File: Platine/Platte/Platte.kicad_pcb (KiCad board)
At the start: 2 copper layers, 32.6 x 32.6 mm, 21 parts, among them J1 Conn_01x07_MountingPin, J3 Conn_01x04_Socket

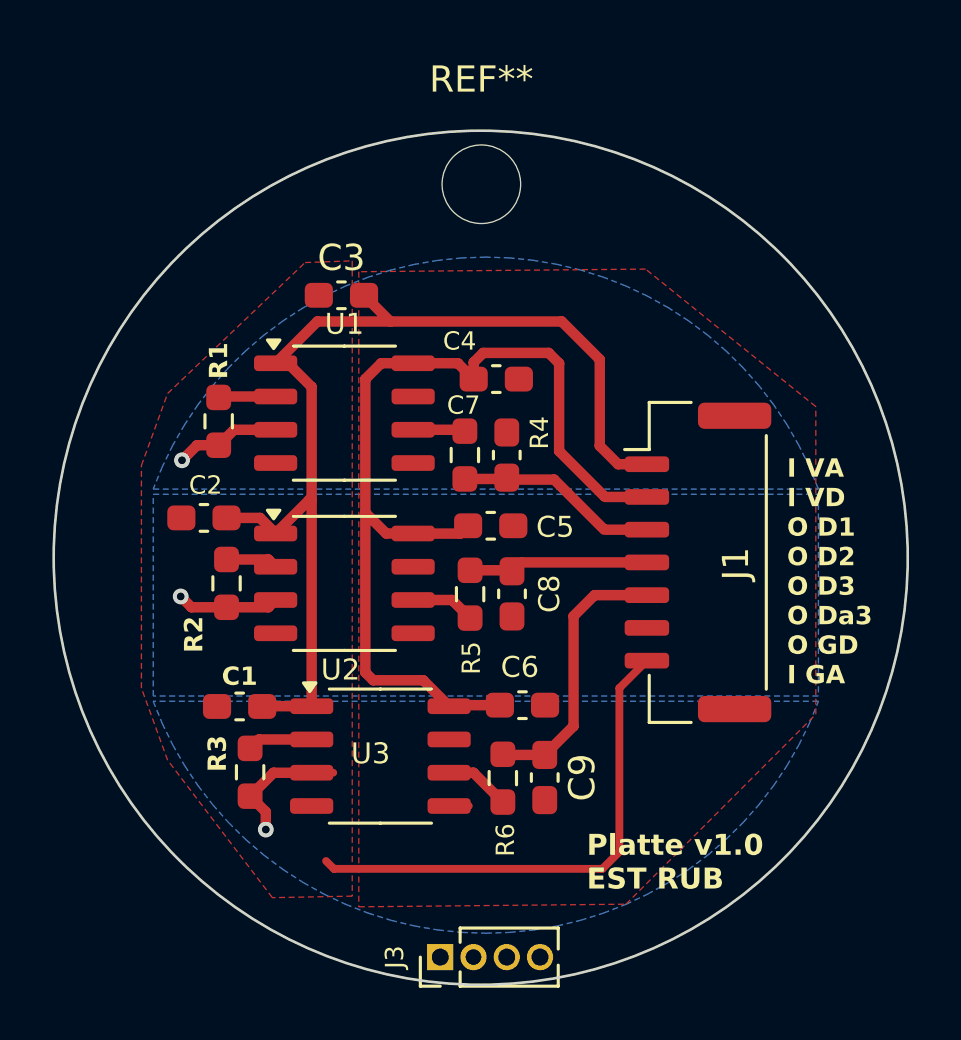
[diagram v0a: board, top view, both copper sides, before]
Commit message: corrections on platte PCB
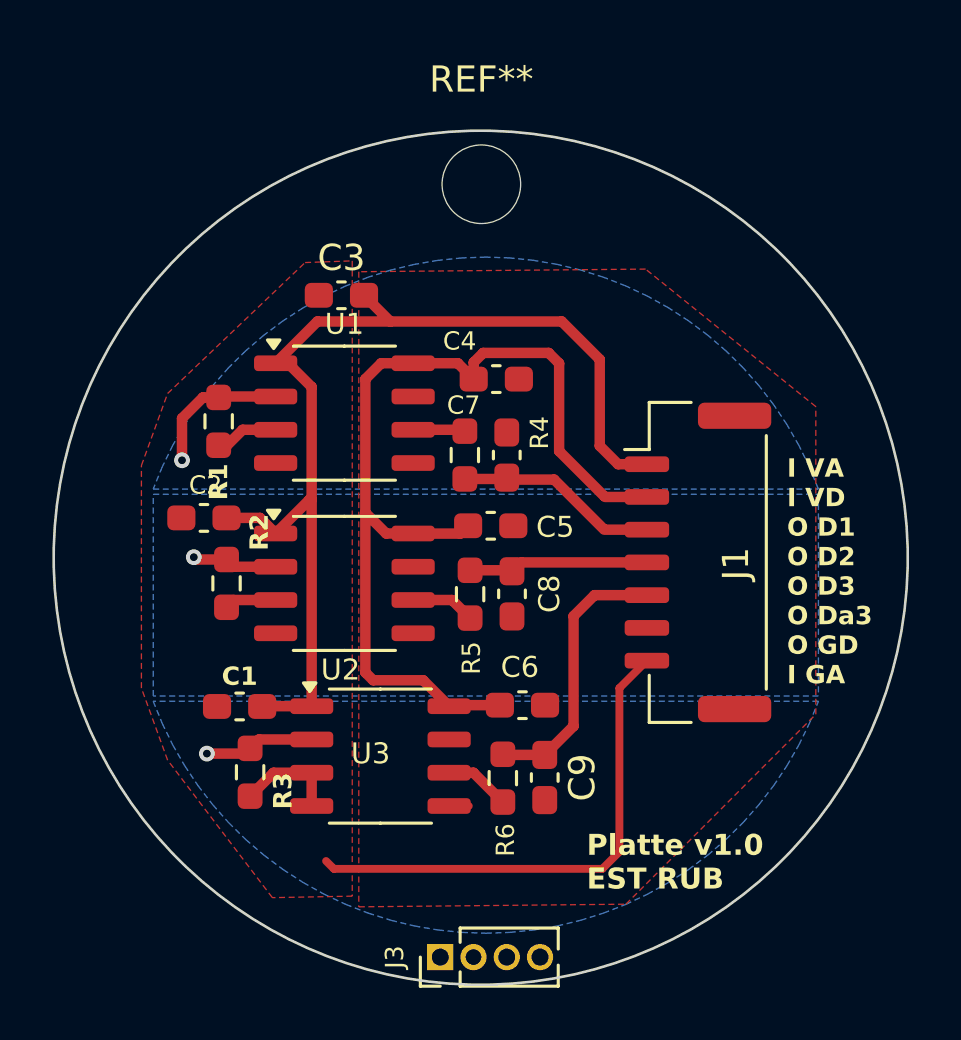
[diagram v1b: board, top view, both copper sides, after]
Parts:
- turned R1 to 90 degrees
- turned R2 to 90 degrees
- turned R3 to 90 degrees
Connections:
- U1 pad 2: GNDA -> /analog_inp_1
- U1 pad 3: /analog_inp_1 -> GNDA
- U2 pad 2: GNDA -> /analog_inp_2
- U2 pad 3: /analog_inp_2 -> GNDA
- U3 pad 2: GNDA -> /analog_inp_3
- U3 pad 3: /analog_inp_3 -> GNDA
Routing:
- net GNDA: track 26.4 -> 28.0 mm
- net /analog_inp_1: track 4.06 -> 5.52 mm
- net /analog_inp_3: track 5.07 -> 4.22 mm
